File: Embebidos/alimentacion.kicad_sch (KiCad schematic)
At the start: 20 parts, among them J4 Conn_01x02_Male, U3 SPX3819M5-L-3-3, U4 MIC29302WT, U5 MIC5219-3.3YM5

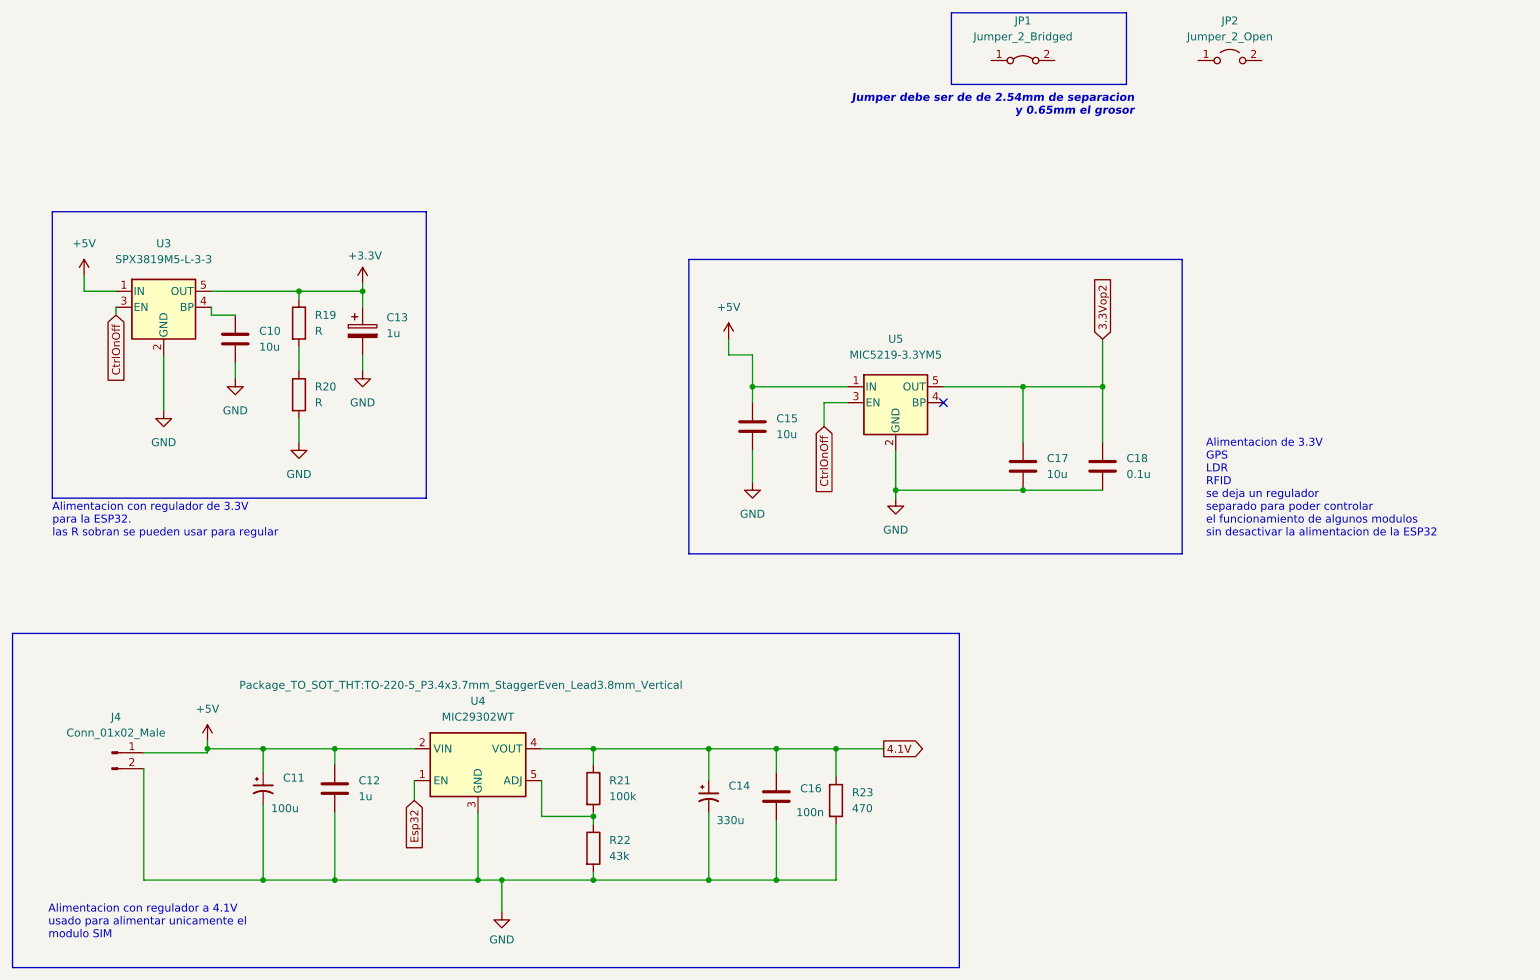
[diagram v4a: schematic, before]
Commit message: Cambios varios
-Conectores movidos a nueva hoja jerarquica

-Transistores DMP colocados en lices delanteras

-Jumpers ubicados para el uso del pin IO13 para SIM800 y LEDHW

-Etiqueta de "no conectado" ubicada en USB_UART
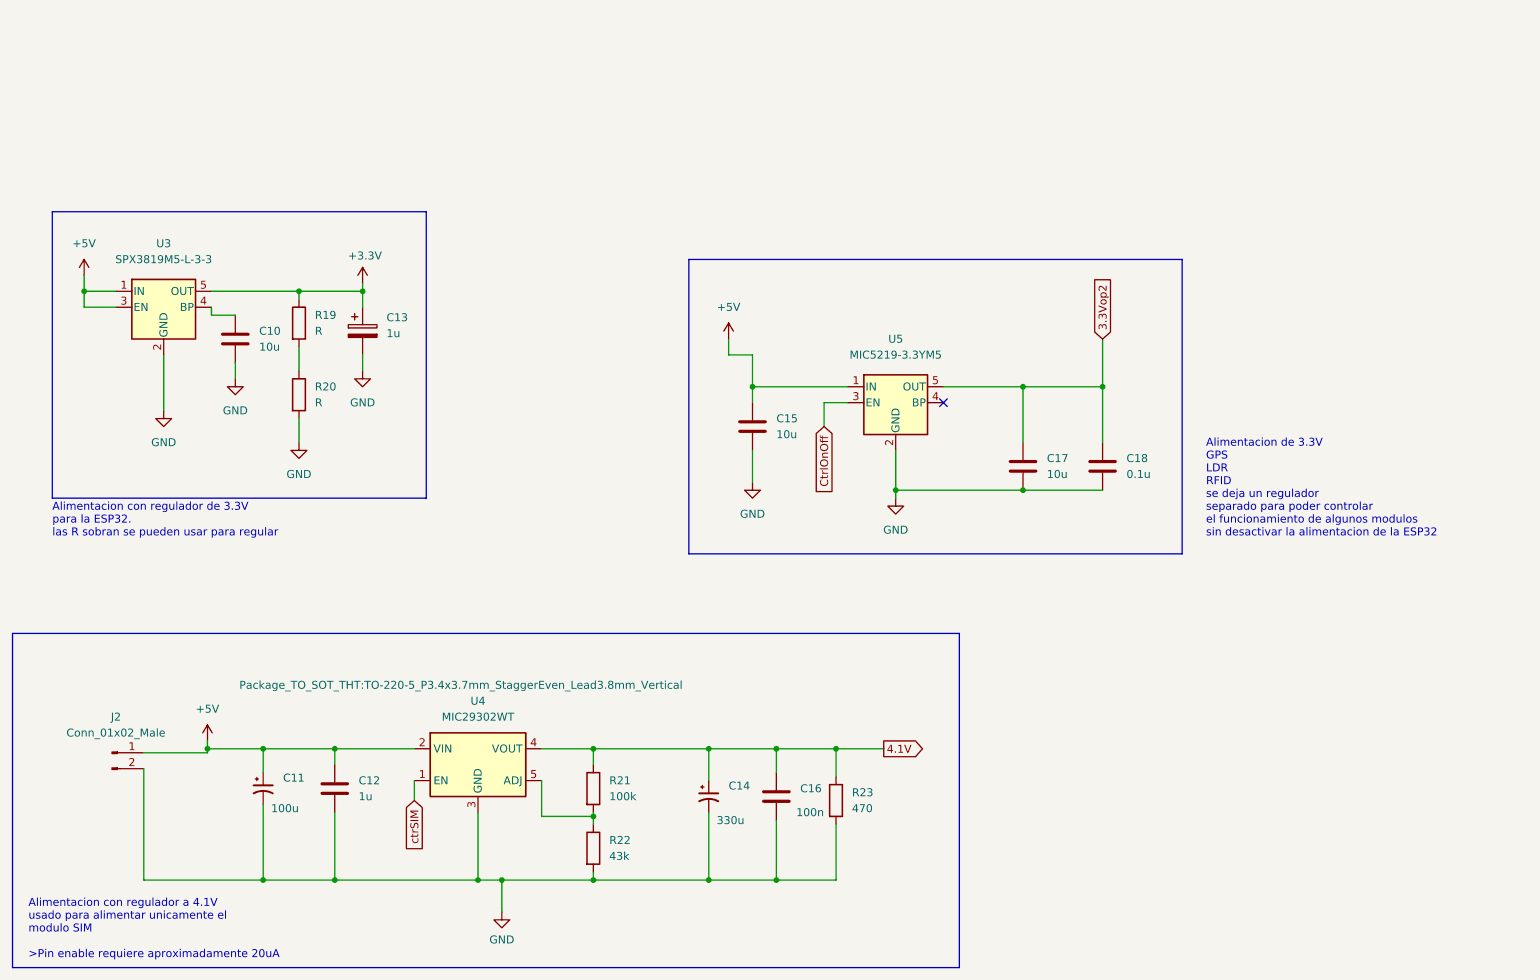
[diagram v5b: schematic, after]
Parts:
- removed JP1: Jumper_2_Bridged, symbol Jumper:Jumper_2_Bridged
- removed JP2: Jumper_2_Open, symbol Jumper:Jumper_2_Open
- renumbered J4 to J2
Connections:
- net +5V: now also U3.3 (EN)
- net CtrlOnOff: no longer U3.3 (EN)
- net Esp32 renamed ctrSIM
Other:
- note added: "Alimentacion con regulador a 4.1V usado para alimentar unicamente el modulo SIM >Pin enable requiere aproximadamente 20uA"
- note removed: "Alimentacion con regulador a 4.1V usado para alimentar unicamente el modulo SIM"
- note removed: "Jumper debe ser de de 2.54mm de separacion y 0.65mm el grosor"
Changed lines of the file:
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@@
   (junction (at 195.58 81.28) (diameter 0) (color 0 0 0 0)
+  )
+  (junction (at 33.02 66.04) (diameter 0) (color 0 0 0 0)
   )
   (junction (at 99.695 160.02) (diameter 0) (color 0 0 0 0)
@@
     (stroke (width 0) (type default) (color 0 0 0 0))
   )
+  (wire (pts (xy 38.1 68.58) (xy 33.02 68.58))
+    (stroke (width 0) (type default) (color 0 0 0 0))
+  )
   (polyline (pts (xy 21.59 120.65) (xy 172.72 120.65))
     (stroke (width 0) (type default) (color 0 0 0 0))
@@
     (stroke (width 0) (type default) (color 0 0 0 0))
   )
-  (polyline (pts (xy 199.39 33.02) (xy 171.45 33.02))
-    (stroke (width 0) (type default) (color 0 0 0 0))
-  )
   (wire (pts (xy 114.3 158.75) (xy 114.3 160.02))
     (stroke (width 0) (type default) (color 0 0 0 0))
@@
     (stroke (width 0) (type default) (color 0 0 0 0))
   )
-  (polyline (pts (xy 171.45 21.59) (xy 171.45 33.02))
-    (stroke (width 0) (type default) (color 0 0 0 0))
-  )
   (wire (pts (xy 57.15 77.47) (xy 57.15 80.01))
     (stroke (width 0) (type default) (color 0 0 0 0))
@@
     (stroke (width 0) (type default) (color 0 0 0 0))
   )
+  (wire (pts (xy 33.02 68.58) (xy 33.02 66.04))
+    (stroke (width 0) (type default) (color 0 0 0 0))
+  )
   (polyline (pts (xy 129.54 60.96) (xy 208.28 60.96))
     (stroke (width 0) (type default) (color 0 0 0 0))
@@
     (stroke (width 0) (type default) (color 0 0 0 0))
   )
-  (polyline (pts (xy 199.39 21.59) (xy 199.39 33.02))
-    (stroke (width 0) (type default) (color 0 0 0 0))
-  )
   (wire (pts (xy 114.3 149.86) (xy 106.045 149.86))
     (stroke (width 0) (type default) (color 0 0 0 0))
@@
     (stroke (width 0) (type default) (color 0 0 0 0))
   )
-  (polyline (pts (xy 171.45 21.59) (xy 199.39 21.59))
-    (stroke (width 0) (type default) (color 0 0 0 0))
-  )
   (wire (pts (xy 135.89 73.66) (xy 135.89 76.2))
     (stroke (width 0) (type default) (color 0 0 0 0))
@@
   )
   (wire (pts (xy 42.545 142.24) (xy 42.545 160.02))
-    (stroke (width 0) (type default) (color 0 0 0 0))
-  )
-  (wire (pts (xy 38.1 69.85) (xy 38.1 68.58))
     (stroke (width 0) (type default) (color 0 0 0 0))
   )
@@
     (effects (font (size 1.27 1.27)) (justify left bottom))
   )
-  (text "Alimentacion con regulador a 4.1V \nusado para alimentar unicamente el\nmodulo SIM\n"
-    (at 27.305 169.545 0)
+  (text "Alimentacion con regulador a 4.1V \nusado para alimentar unicamente el\nmodulo SIM\n\n>Pin enable requiere aproximadamente 20uA"
+    (at 24.13 172.72 0)
     (effects (font (size 1.27 1.27)) (justify left bottom))
   )
@@
     (at 27.94 105.41 0)
     (effects (font (size 1.27 1.27)) (justify left bottom))
-  )
-  (text "Jumper debe ser de de 2.54mm de separacion\n y 0.65mm el grosor"
-    (at 200.66 38.1 0)
-    (effects (font (size 1.27 1.27) (thickness 0.254) bold italic) (justify right bottom))
   )
   (global_label "3.3Vop2" (shape input) (at 195.58 73.66 90) (fields_autoplaced)
@@
     )
   )
-  (global_label "CtrlOnOff" (shape input) (at 38.1 69.85 270) (fields_autoplaced)
-    (effects (font (size 1.27 1.27)) (justify right))
-    (property "Intersheet References" "${INTERSHEET_REFS}" (id 0) (at 38.0206 80.9717 90)
-      (effects (font (size 1.27 1.27)) (justify right) hide)
-    )
-  )
   (global_label "4.1V" (shape output) (at 160.655 139.065 0) (fields_autoplaced)
     (effects (font (size 1.27 1.27)) (justify left))
@@
     )
   )
-  (global_label "Esp32" (shape input) (at 85.725 147.32 270) (fields_autoplaced)
+  (global_label "ctrSIM" (shape input) (at 85.725 147.32 270) (fields_autoplaced)
     (effects (font (size 1.27 1.27)) (justify right))
-    (property "Intersheet References" "${INTERSHEET_REFS}" (id 0) (at 85.6456 155.4783 90)
+    (property "Intersheet References" "${INTERSHEET_REFS}" (id 0) (at 85.6456 155.5993 90)
       (effects (font (size 1.27 1.27)) (justify right) hide)
     )
@@
   (symbol (lib_id "power:GND") (at 99.695 165.1 0) (unit 1)
     (in_bom yes) (on_board yes) (fields_autoplaced)
-    (property "Reference" "#PWR031" (id 0) (at 99.695 171.45 0)
+    (property "Reference" "#PWR028" (id 0) (at 99.695 171.45 0)
       (effects (font (size 1.27 1.27)) hide)
     )
@@
   (symbol (lib_id "power:GND") (at 67.31 90.17 0) (unit 1)
     (in_bom yes) (on_board yes) (fields_autoplaced)
-    (property "Reference" "#PWR028" (id 0) (at 67.31 96.52 0)
+    (property "Reference" "#PWR025" (id 0) (at 67.31 96.52 0)
       (effects (font (size 1.27 1.27)) hide)
     )
@@
   (symbol (lib_id "power:GND") (at 139.7 96.52 0) (unit 1)
     (in_bom yes) (on_board yes) (fields_autoplaced)
-    (property "Reference" "#PWR033" (id 0) (at 139.7 102.87 0)
+    (property "Reference" "#PWR030" (id 0) (at 139.7 102.87 0)
       (effects (font (size 1.27 1.27)) hide)
     )
@@
   (symbol (lib_id "power:GND") (at 57.15 80.01 0) (unit 1)
     (in_bom yes) (on_board yes) (fields_autoplaced)
-    (property "Reference" "#PWR027" (id 0) (at 57.15 86.36 0)
+    (property "Reference" "#PWR024" (id 0) (at 57.15 86.36 0)
       (effects (font (size 1.27 1.27)) hide)
     )
@@
   (symbol (lib_id "power:GND") (at 162.56 99.06 0) (unit 1)
     (in_bom yes) (on_board yes) (fields_autoplaced)
-    (property "Reference" "#PWR034" (id 0) (at 162.56 105.41 0)
+    (property "Reference" "#PWR031" (id 0) (at 162.56 105.41 0)
       (effects (font (size 1.27 1.27)) hide)
     )
@@
   (symbol (lib_id "power:GND") (at 77.47 78.74 0) (unit 1)
     (in_bom yes) (on_board yes) (fields_autoplaced)
-    (property "Reference" "#PWR030" (id 0) (at 77.47 85.09 0)
+    (property "Reference" "#PWR027" (id 0) (at 77.47 85.09 0)
       (effects (font (size 1.27 1.27)) hide)
     )
@@
   (symbol (lib_id "power:+3.3V") (at 77.47 64.77 0) (unit 1)
     (in_bom yes) (on_board yes)
-    (property "Reference" "#PWR029" (id 0) (at 77.47 68.58 0)
+    (property "Reference" "#PWR026" (id 0) (at 77.47 68.58 0)
       (effects (font (size 1.27 1.27)) hide)
     )
@@
   (symbol (lib_id "power:GND") (at 45.72 85.09 0) (unit 1)
     (in_bom yes) (on_board yes) (fields_autoplaced)
-    (property "Reference" "#PWR025" (id 0) (at 45.72 91.44 0)
+    (property "Reference" "#PWR022" (id 0) (at 45.72 91.44 0)
       (effects (font (size 1.27 1.27)) hide)
     )
@@
     (pin "2")
   )
-  (symbol (lib_id "Jumper:Jumper_2_Open") (at 215.9 29.21 0) (unit 1)
-    (in_bom yes) (on_board yes) (fields_autoplaced)
-    (property "Reference" "JP2" (id 0) (at 215.9 22.86 0))
-    (property "Value" "Jumper_2_Open" (id 1) (at 215.9 25.4 0))
-    (property "Footprint" "" (id 2) (at 215.9 29.21 0)
-      (effects (font (size 1.27 1.27)) hide)
-    )
-    (property "Datasheet" "~" (id 3) (at 215.9 29.21 0)
-      (effects (font (size 1.27 1.27)) hide)
-    )
-    (pin "1")
-    (pin "2")
-  )
   (symbol (lib_id "power:+5V") (at 135.89 73.66 0) (unit 1)
     (in_bom yes) (on_board yes) (fields_autoplaced)
-    (property "Reference" "#PWR032" (id 0) (at 135.89 77.47 0)
+    (property "Reference" "#PWR029" (id 0) (at 135.89 77.47 0)
       (effects (font (size 1.27 1.27)) hide)
     )
@@
   (symbol (lib_id "power:+5V") (at 33.02 63.5 0) (unit 1)
     (in_bom yes) (on_board yes) (fields_autoplaced)
-    (property "Reference" "#PWR024" (id 0) (at 33.02 67.31 0)
+    (property "Reference" "#PWR021" (id 0) (at 33.02 67.31 0)
       (effects (font (size 1.27 1.27)) hide)
     )
@@
   (symbol (lib_id "Connector:Conn_01x02_Male") (at 37.465 139.7 0) (unit 1)
     (in_bom yes) (on_board yes) (fields_autoplaced)
-    (property "Reference" "J4" (id 0) (at 38.1 133.985 0))
+    (property "Reference" "J2" (id 0) (at 38.1 133.985 0))
     (property "Value" "Conn_01x02_Male" (id 1) (at 38.1 136.525 0))
     (property "Footprint" "" (id 2) (at 37.465 139.7 0)
@@
     (pin "2")
   )
-  (symbol (lib_id "Jumper:Jumper_2_Bridged") (at 182.88 29.21 0) (unit 1)
-    (in_bom yes) (on_board yes) (fields_autoplaced)
-    (property "Reference" "JP1" (id 0) (at 182.88 22.86 0))
-    (property "Value" "Jumper_2_Bridged" (id 1) (at 182.88 25.4 0))
-    (property "Footprint" "" (id 2) (at 182.88 29.21 0)
-      (effects (font (size 1.27 1.27)) hide)
-    )
-    (property "Datasheet" "~" (id 3) (at 182.88 29.21 0)
-      (effects (font (size 1.27 1.27)) hide)
-    )
-    (pin "1")
-    (pin "2")
-  )
   (symbol (lib_id "Device:C") (at 182.88 93.98 0) (unit 1)
     (in_bom yes) (on_board yes) (fields_autoplaced)
@@
   (symbol (lib_id "power:+5V") (at 52.705 137.795 0) (unit 1)
     (in_bom yes) (on_board yes) (fields_autoplaced)
-    (property "Reference" "#PWR026" (id 0) (at 52.705 141.605 0)
-      (effects (font (size 1.27 1.27)) hide)
-    )
+    (property "Reference" "#PWR023" (id 0) (at 52.705 141.605 0)
+      (effects (font (size 1.27 1.27)) hide)
+    )
